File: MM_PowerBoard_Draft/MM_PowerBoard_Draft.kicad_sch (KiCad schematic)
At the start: 13 parts, among them J1 JST_Battery, J2 2x16_Motherboard, J3 USB_C_Receptacle, Q1 PMOS, SW1 SW_SPDT, U1 CYPD3177-24LQ, U2 LGS5500EP, U4 AP2112K-3.3, U5 TPS63061

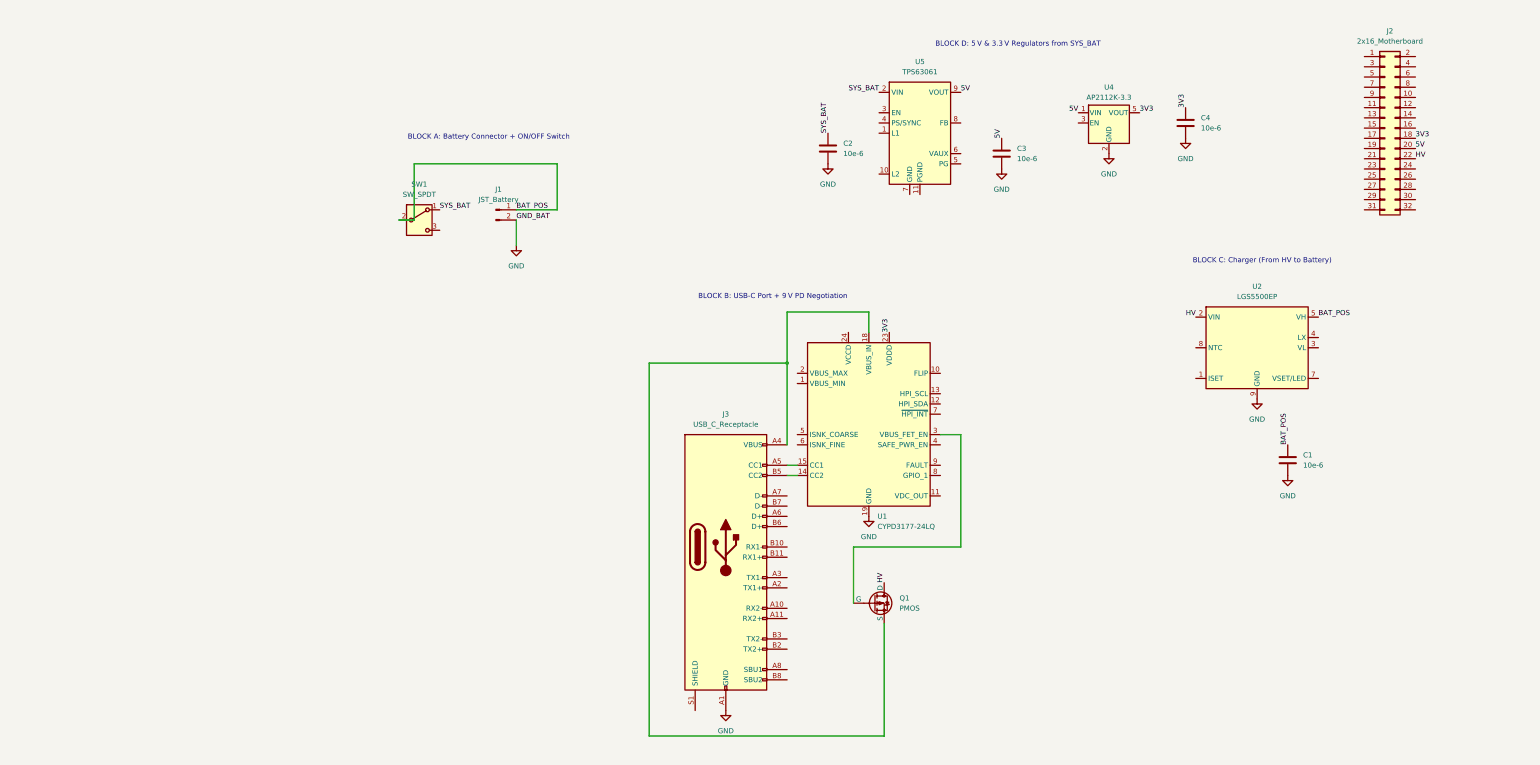
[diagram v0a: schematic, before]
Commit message: Added preliminary 1. Motor Drivers 2. Battery Sensing 3. Board Header
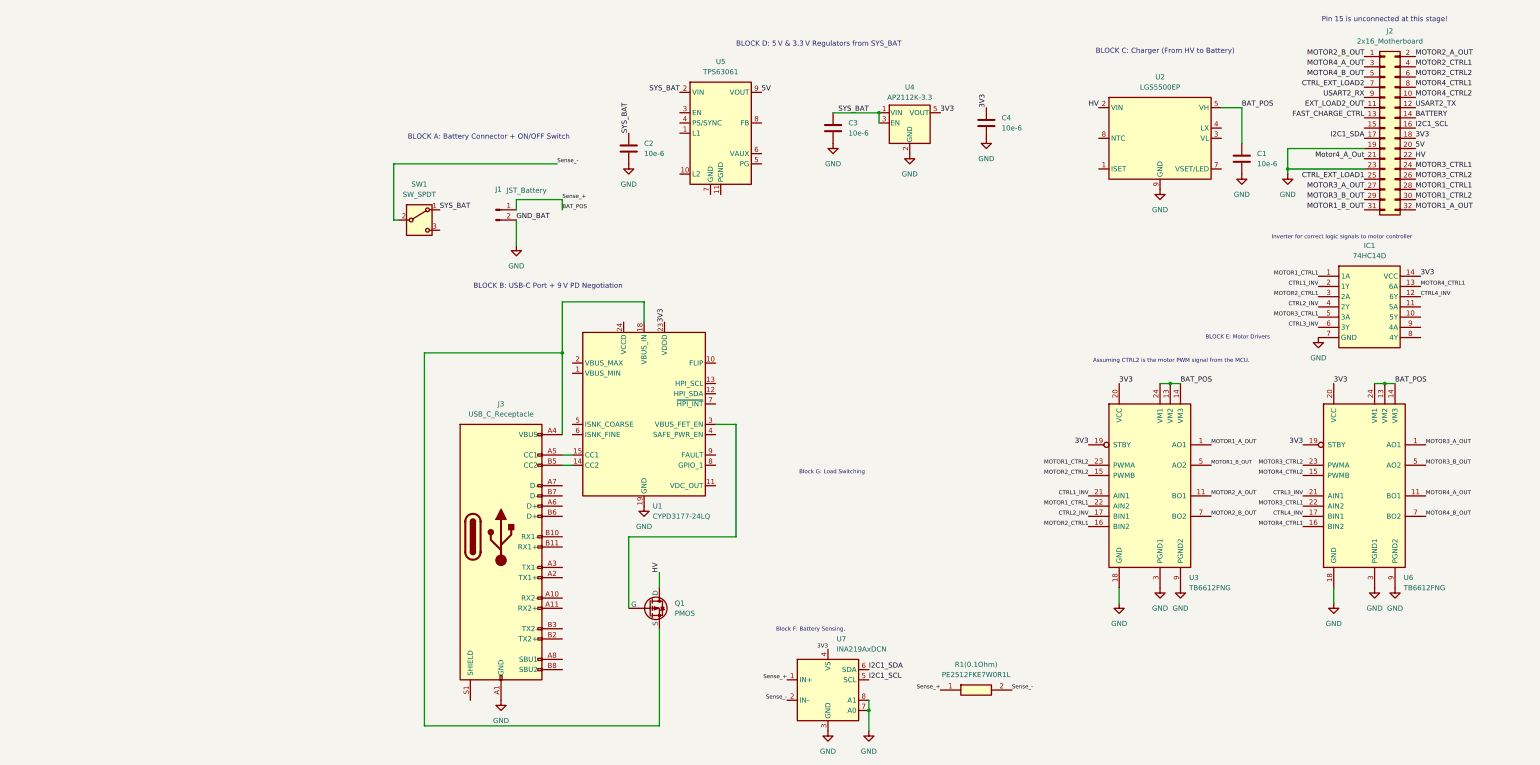
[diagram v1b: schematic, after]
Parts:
- added IC1: 74HC14D, Package_SO:SOIC-14_3.9x8.7mm_P1.27mm, symbol 74HC14D:74HC14D
- added R1(0.1Ohm): PE2512FKE7W0R1L, Current_Sense:RESC6432X89N, symbol 0.1 Ohm current sense:PE2512FKE7W0R1L
- added U3, U6: TB6612FNG, Package_SO:SSOP-24_5.3x8.2mm_P0.65mm, symbol Driver_Motor:TB6612FNG
- added U7: INA219AxDCN, Package_TO_SOT_SMD:SOT-23-8, symbol Sensor_Energy:INA219AxDCN
- J2: footprint (none) -> Connector_PinHeader_2.54mm:PinHeader_2x16_P2.54mm_Vertical
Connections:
- net 3V3: now also IC1.14 (VCC), U3.19 (STBY), U3.20 (VCC), U6.19 (STBY), U6.20 (VCC), U7.4 (VS)
- net 5V: no longer C3.1, U4.1 (VIN)
- net BAT_POS: now also R1(0.1Ohm).1, U3.13 (VM2), U3.14 (VM3), U3.24 (VM1), U6.13 (VM2), U6.14 (VM3), U6.24 (VM1), U7.1 (IN+); no longer SW1.2 (B)
- net GND: now also J2.19 (Pin_19), J2.23 (Pin_23), IC1.7 (GND), U3.10 (PGND2), U3.18 (GND), U3.3 (PGND1), U3.4 (PGND1), U3.9 (PGND2), U6.10 (PGND2), U6.18 (GND), U6.3 (PGND1), U6.4 (PGND1), U6.9 (PGND2), U7.3 (GND), U7.7 (A0), U7.8 (A1)
- net SYS_BAT: now also C3.1, U4.1 (VIN), U4.3 (EN)
- net MOTOR2_B_OUT: now reaches J2.1 (Pin_1)
- net MOTOR2_B_OUT: now also U3.7 (BO2), U3.8 (BO2)
- net MOTOR4_CTRL2: now reaches J2.10 (Pin_10)
- net MOTOR4_CTRL2: now also U6.15 (PWMB)
- net EXT_LOAD2_OUT: now reaches J2.11 (Pin_11)
- net USART2_TX: now reaches J2.12 (Pin_12)
- net FAST_CHARGE_CTRL: now reaches J2.13 (Pin_13)
- net BATTERY: now reaches J2.14 (Pin_14)
- net I2C1_SCL: now reaches J2.16 (Pin_16)
- net I2C1_SCL: now also U7.5 (SCL)
- net I2C1_SDA: now reaches J2.17 (Pin_17)
- net I2C1_SDA: now also U7.6 (SDA)
- net MOTOR2_A_OUT: now reaches J2.2 (Pin_2)
- net MOTOR2_A_OUT: now also U3.11 (BO1), U3.12 (BO1)
- net Motor4_A_Out: now reaches J2.21 (Pin_21)
- net MOTOR3_CTRL1: now reaches J2.24 (Pin_24)
- net MOTOR3_CTRL1: now also IC1.5 (3A), U6.22 (AIN2)
- net CTRL_EXT_LOAD1: now reaches J2.25 (Pin_25)
- net MOTOR3_CTRL2: now reaches J2.26 (Pin_26)
- net MOTOR3_CTRL2: now also U6.23 (PWMA)
- net MOTOR3_A_OUT: now reaches J2.27 (Pin_27)
- net MOTOR3_A_OUT: now also U6.1 (AO1), U6.2 (AO1)
- net MOTOR1_CTRL1: now reaches J2.28 (Pin_28)
- net MOTOR1_CTRL1: now also IC1.1 (1A), U3.22 (AIN2)
- net MOTOR3_B_OUT: now reaches J2.29 (Pin_29)
- net MOTOR3_B_OUT: now also U6.5 (AO2), U6.6 (AO2)
- net MOTOR4_A_OUT: now reaches J2.3 (Pin_3)
- net MOTOR4_A_OUT: now also U6.11 (BO1), U6.12 (BO1)
- net MOTOR1_CTRL2: now reaches J2.30 (Pin_30)
- net MOTOR1_CTRL2: now also U3.23 (PWMA)
- net MOTOR1_B_OUT: now reaches J2.31 (Pin_31)
- net MOTOR1_B_OUT: now also U3.5 (AO2), U3.6 (AO2)
- net MOTOR1_A_OUT: now reaches J2.32 (Pin_32)
- net MOTOR1_A_OUT: now also U3.1 (AO1), U3.2 (AO1)
- net MOTOR2_CTRL1: now reaches J2.4 (Pin_4)
- net MOTOR2_CTRL1: now also IC1.3 (2A), U3.16 (BIN2)
- net MOTOR4_B_OUT: now reaches J2.5 (Pin_5)
- net MOTOR4_B_OUT: now also U6.7 (BO2), U6.8 (BO2)
- net MOTOR2_CTRL2: now reaches J2.6 (Pin_6)
- net MOTOR2_CTRL2: now also U3.15 (PWMB)
- net CTRL_EXT_LOAD2: now reaches J2.7 (Pin_7)
- net MOTOR4_CTRL1: now reaches J2.8 (Pin_8)
- net MOTOR4_CTRL1: now also IC1.13 (6A), U6.16 (BIN2)
- net USART2_RX: now reaches J2.9 (Pin_9)
- new net CTRL1_INV: IC1.2 (1Y), U3.21 (AIN1)
- new net CTRL2_INV: IC1.4 (2Y), U3.17 (BIN1)
- new net CTRL3_INV: IC1.6 (3Y), U6.21 (AIN1)
- new net CTRL4_INV: IC1.12 (6Y), U6.17 (BIN1)
- new net Sense_-: R1(0.1Ohm).2, SW1.2 (B), U7.2 (IN-)
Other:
- note added: "Assuming CTRL2 is the motor PWM signal from the MCU."
- note added: "BLOCK E: Motor Drivers"
- note added: "Block F: Battery Sensing."
- note added: "Block G: Load Switching"
- note added: "Inverter for correct logic signals to motor controller"
- note added: "Pin 15 is unconnected at this stage!"
- title: (none) -> Power Subboard Design
- moved on the sheet: C1, C2, C3, C4, J3, Q1, U1, U2, U4, U5

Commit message: Added battery charger which handles load switch over when external power source is plugged in.
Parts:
- removed U2: LGS5500EP, Package_SO:SOIC-8-1EP_3.9x4.9mm_P1.27mm_EP2.41x3.3mm, symbol Battery_Management:LGS5500EP
- added C5: 4.7e-6, symbol Device:C
- added C6: 10e-6, symbol Device:C
- added Q2: AO3400A, Package_TO_SOT_SMD:SOT-23, symbol Transistor_FET:AO3400A
- added R1, R2: 1.5k, symbol Device:R_US
- added R3: 1.1k, symbol Device:R_US
- added R4: 10k, symbol Device:R_US
- added R5: 4.7k, Resistor_SMD:R_0603_1608Metric, symbol Device:R_US
- added R6: 2.2k, Resistor_SMD:R_0603_1608Metric, symbol Device:R_US
- added U8: BQ24074RGT, Package_DFN_QFN:VQFN-16-1EP_3x3mm_P0.5mm_EP1.6x1.6mm, symbol Battery_Management:BQ24074RGT
- C1: value 10e-6 -> 1e-6
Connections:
- net BAT_POS: no longer C1.1
- net FAST_CHARGE_CTRL: now also Q2.1 (G)
- net GND: now also C5.2, C6.2, Q2.2 (S), R3.1, R4.2, R5.2, U8.14 (TMR), U8.17 (VSS), U8.4 (~{CE}), U8.6 (EN1), U8.8 (VSS)
- net HV: now also C1.1, U8.13 (IN)
- net SYS_BAT: now also C6.1, U8.2 (BAT), U8.3 (BAT); no longer C2.1, C3.1, U4.1 (VIN), U4.3 (EN), U5.2 (VIN)
- new net: R4.1, U8.1 (TS)
- new net: Q2.3 (D), R6.2
- new net: R1.1, U8.9 (~{CHG})
- new net: R5.1, R6.1, U8.16 (ISET)
- new net: R3.2, U8.12 (ILIM)
- new net: R2.1, U8.7 (~{PGOOD})
- new net Out: C2.1, C3.1, C5.1, R1.2, R2.2, U4.1 (VIN), U4.3 (EN), U5.2 (VIN), U8.10 (OUT), U8.11 (OUT), U8.5 (EN2)
- no-connect marks 0 -> 1
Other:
- moved on the sheet: C4

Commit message: testing
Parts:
- added L1: L, symbol Device:L
- added Q3, Q4: PMOS, symbol Simulation_SPICE:PMOS
- added R7, R8: 100k, symbol Device:R_US
- added U9: TPS613222ADBZ, Package_TO_SOT_SMD:SOT-23, symbol Regulator_Switching:TPS613222ADBZ
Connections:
- net 5V: now also Q3.3 (S), Q4.3 (S), R7.1, R8.1, U9.1 (VOUT)
- net CTRL_EXT_LOAD1: now also Q3.2 (G), R7.2
- net CTRL_EXT_LOAD2: now also Q4.2 (G), R8.2
- net EXT_LOAD2_OUT: now also Q4.1 (D)
- net GND: now also U9.3 (GND)
- net Out: now also L1.1, L1.2, U9.2 (SW)
- new net EXT_LOAD1_OUT: Q3.1 (D)
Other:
- moved on the sheet: U5

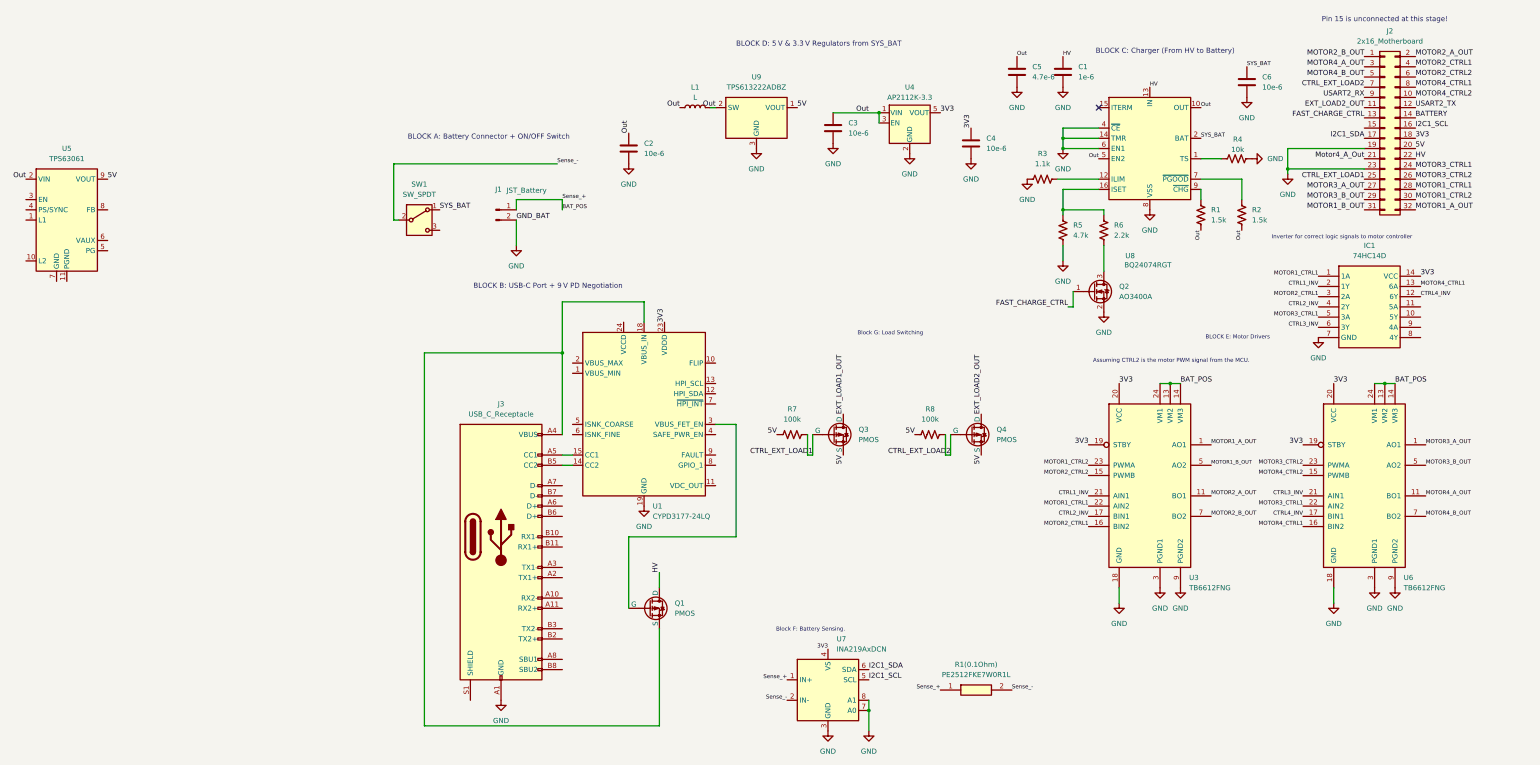
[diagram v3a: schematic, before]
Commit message: Load switching fixed
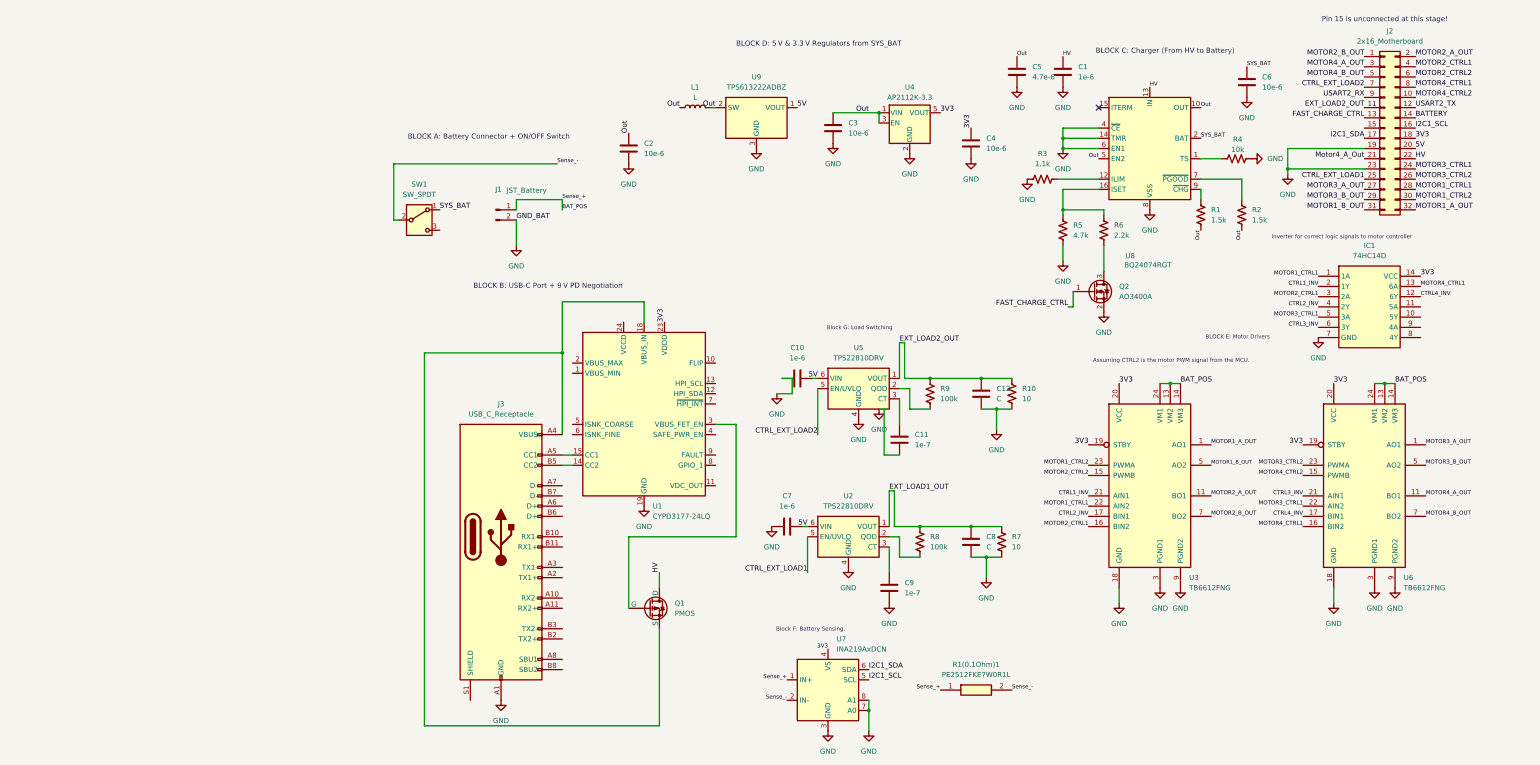
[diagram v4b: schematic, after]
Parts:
- removed Q3, Q4: PMOS, symbol Simulation_SPICE:PMOS
- removed U5: TPS63061, Package_SON:Texas_S-PWSON-N10_ThermalVias, symbol Regulator_Switching:TPS63061
- added C10, C7: 1e-6, symbol Device:C
- added C11, C9: 1e-7, symbol Device:C
- added C12, C8: C, symbol Device:C
- added R10: 10, symbol Device:R_US
- added R9: 100k, symbol Device:R_US
- added U2, U5: TPS22810DRV, Package_SON:WSON-6-1EP_2x2mm_P0.65mm_EP1x1.6mm, symbol Power_Management:TPS22810DRV
- R7: value 100k -> 10
- renumbered R1(0.1Ohm) to R1(0.1Ohm)1
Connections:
- net 5V: now also C10.2, C7.2, U2.6 (VIN), U5.6 (VIN); no longer R7.1, R8.1
- net CTRL_EXT_LOAD1: now also U2.5 (EN/UVLO); no longer R7.2
- net CTRL_EXT_LOAD2: now also U5.5 (EN/UVLO); no longer R8.2
- net EXT_LOAD1_OUT: now also R7.1, R8.1, C8.1, U2.1 (VOUT)
- net EXT_LOAD2_OUT: now also C12.1, R10.1, R9.1, U5.1 (VOUT)
- net GND: now also R7.2, C10.1, C11.2, C12.2, C7.1, C8.2, C9.2, R10.2, U2.4 (GND), U2.7 (GND), U5.4 (GND), U5.7 (GND)
- new net: C11.1, U5.3 (CT)
- new net: R8.2, U2.2 (QOD)
- new net: C9.1, U2.3 (CT)
- new net: R9.2, U5.2 (QOD)

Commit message: Fixed some stuff
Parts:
- C11: value 1e-7 -> 2200e-12
- C12, C8: value C -> 1e-7
- C9: value 1e-7 -> 2200e-9
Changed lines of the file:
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@@
 			)
 		)
-		(property "Value" "1e-7"
+		(property "Value" "2200e-12"
 			(at 144.78 120.6499 0)
 			(effects
@@
 			)
 		)
-		(property "Value" "C"
+		(property "Value" "1e-7"
 			(at 162.56 146.0499 0)
 			(effects
@@
 			)
 		)
-		(property "Value" "C"
+		(property "Value" "1e-7"
 			(at 165.1 109.2199 0)
 			(effects
@@
 			)
 		)
-		(property "Value" "1e-7"
+		(property "Value" "2200e-9"
 			(at 142.24 157.4799 0)
 			(effects

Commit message: Added some footprints
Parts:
- C1, C10, C11, C12, C2, C3, C4, C5, C6, C7, C8, C9: footprint (none) -> Capacitor_SMD:C_0805_2012Metric
- J1: footprint (none) -> Connector_JST:JST_PH_S2B-PH-SM4-TB_1x02-1MP_P2.00mm_Horizontal
- L1: footprint (none) -> Inductor_SMD:L_0805_2012Metric
- R1, R10, R2, R3, R4, R7, R8, R9: footprint (none) -> Resistor_SMD:R_0603_1608Metric
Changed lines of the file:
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@@
 			)
 		)
-		(property "Footprint" ""
+		(property "Footprint" "Capacitor_SMD:C_0805_2012Metric"
 			(at 141.9352 123.19 0)
 			(effects
@@
 			)
 		)
-		(property "Footprint" ""
+		(property "Footprint" "Resistor_SMD:R_0603_1608Metric"
 			(at 225.044 48.514 90)
 			(effects
@@
 			)
 		)
-		(property "Footprint" ""
+		(property "Footprint" "Resistor_SMD:R_0603_1608Metric"
 			(at 167.386 145.034 90)
 			(effects
@@
 			)
 		)
-		(property "Footprint" ""
+		(property "Footprint" "Capacitor_SMD:C_0805_2012Metric"
 			(at 228.2952 34.29 0)
 			(effects
@@
 			)
 		)
-		(property "Footprint" ""
+		(property "Footprint" "Resistor_SMD:R_0603_1608Metric"
 			(at 216.916 63.754 90)
 			(effects
@@
 			)
 		)
-		(property "Footprint" ""
+		(property "Footprint" "Capacitor_SMD:C_0805_2012Metric"
 			(at 182.5752 31.75 0)
 			(effects
@@
 			)
 		)
-		(property "Footprint" ""
+		(property "Footprint" "Capacitor_SMD:C_0805_2012Metric"
 			(at 171.1452 31.75 0)
 			(effects
@@
 			)
 		)
-		(property "Footprint" ""
+		(property "Footprint" "Capacitor_SMD:C_0805_2012Metric"
 			(at 159.7152 148.59 0)
 			(effects
@@
 			)
 		)
-		(property "Footprint" ""
+		(property "Footprint" "Capacitor_SMD:C_0805_2012Metric"
 			(at 159.7152 49.53 0)
 			(effects
@@
 			)
 		)
-		(property "Footprint" ""
+		(property "Footprint" "Resistor_SMD:R_0603_1608Metric"
 			(at 147.066 145.034 90)
 			(effects
@@
 			)
 		)
-		(property "Footprint" ""
+		(property "Footprint" "Capacitor_SMD:C_0805_2012Metric"
 			(at 116.84 140.0048 0)
 			(effects
@@
 			)
 		)
-		(property "Footprint" ""
+		(property "Footprint" "Capacitor_SMD:C_0805_2012Metric"
 			(at 74.6252 50.8 0)
 			(effects
@@
 			)
 		)
-		(property "Footprint" ""
+		(property "Footprint" "Resistor_SMD:R_0603_1608Metric"
 			(at 169.926 108.204 90)
 			(effects
@@
 			)
 		)
-		(property "Footprint" ""
+		(property "Footprint" "Capacitor_SMD:C_0805_2012Metric"
 			(at 125.4252 45.72 0)
 			(effects
@@
 			)
 		)
-		(property "Footprint" ""
+		(property "Footprint" "Capacitor_SMD:C_0805_2012Metric"
 			(at 162.2552 111.76 0)
 			(effects
@@
 			)
 		)
-		(property "Footprint" ""
+		(property "Footprint" "Resistor_SMD:R_0603_1608Metric"
 			(at 176.784 53.594 90)
 			(effects
@@
 			)
 		)
-		(property "Footprint" ""
+		(property "Footprint" "Resistor_SMD:R_0603_1608Metric"
 			(at 149.606 108.204 90)
 			(effects
@@
 			)
 		)
-		(property "Footprint" ""
+		(property "Footprint" "Inductor_SMD:L_0805_2012Metric"
 			(at 90.17 36.83 0)
 			(effects
@@
 			)
 		)
-		(property "Footprint" ""
+		(property "Footprint" "Capacitor_SMD:C_0805_2012Metric"
 			(at 139.3952 160.02 0)
 			(effects
@@
 			)
 		)
-		(property "Footprint" ""
+		(property "Footprint" "Connector_JST:JST_PH_S2B-PH-SM4-TB_1x02-1MP_P2.00mm_Horizontal"
 			(at 40.64 62.23 0)
 			(effects
@@
 			)
 		)
-		(property "Footprint" ""
+		(property "Footprint" "Resistor_SMD:R_0603_1608Metric"
 			(at 227.076 63.754 90)
 			(effects
@@
 			)
 		)
-		(property "Footprint" ""
+		(property "Footprint" "Capacitor_SMD:C_0805_2012Metric"
 			(at 119.38 103.1748 0)
 			(effects
